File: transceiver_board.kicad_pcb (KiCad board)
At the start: 2 copper layers, 127 parts, among them J1 RJ45_LED_Shielded, J2 Conn_01x01_Male, J3 SMA_Connector, J4 Conn_01x01_Male, J5 SMA_Connector, Q1 BC547, Q2 BC547, T1 S558-5999-46-F, U1 LAN83C185-JT, U2 ltc6752ims8-2-pbf, U4 AP63203WU, U5 AP63205WU, U6 LM317_TO-220, U7 LM317_TO-220, Y1 25 MHz

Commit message: Begin placing components
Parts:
- moved C43 133.5 mm to (240.0, 150.0)
- moved RV1 133.3 mm to (236.3, 30.7), turned to 180 degrees
- moved C44 131.2 mm to (236.4, 149.4)
- moved R1 130.4 mm to (240.4, 152.6)
- moved R3 128.0 mm to (233.0, 151.6)
- moved C42 125.5 mm to (216.2, 151.0), turned to -90 degrees
- moved R2 121.1 mm to (212.0, 151.0), turned to 90 degrees
- moved C17 114.2 mm to (196.8, 147.4), turned to -90 degrees
- moved R46 112.0 mm to (210.8, 147.6)
- moved RV3 110.7 mm to (233.9, 155.7)
- moved R10 109.5 mm to (30.0, 74.0)
- moved R6 109.5 mm to (30.0, 76.9)
- moved C23 107.1 mm to (231.5, 45.8)
- moved U6 106.7 mm to (213.4, 140.8), turned to 180 degrees
- moved U7 105.1 mm to (234.9, 144.7)
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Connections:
- net PHY-VSS renamed GND
- Q1 pad 3: Net-(J3-Pad1) -> Net-(Q1-Pad3)
- Q2 pad 3: Net-(J3-Pad1) -> Net-(Q1-Pad3)

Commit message: positioned power components
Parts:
- removed R4: 0, Resistor_SMD:R_0805_2012Metric_Pad1.20x1.40mm_HandSolder
- added JP5: SolderJumper_2_Bridged, Jumper:SolderJumper-2_P1.3mm_Bridged_Pad1.0x1.5mm, F.Cu at (33.0, 108.5)
- moved C1 88.9 mm to (40.7, 144.5)
- moved C34 79.5 mm to (168.6, 152.9), turned to 180 degrees
- moved C35 78.8 mm to (44.8, 144.5), turned to 180 degrees
- moved U5 78.6 mm to (166.2, 155.8)
- moved C37 78.4 mm to (44.8, 142.2), turned to 180 degrees
- moved U4 74.7 mm to (42.5, 139.2)
- moved C32 72.9 mm to (164.1, 158.6)
- moved C45 72.5 mm to (40.7, 142.2)
- moved C36 71.1 mm to (168.3, 158.6), turned to 180 degrees
- moved C33 70.3 mm to (44.8, 136.4), turned to 180 degrees
- moved C38 69.0 mm to (168.3, 160.8), turned to 180 degrees
- moved L2 68.3 mm to (171.7, 155.7)
- moved L4 66.4 mm to (159.0, 154.9)
- moved L1 63.2 mm to (48.0, 139.7)
- moved L3 61.7 mm to (36.4, 138.9)
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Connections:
- C1 pad 2: GND -> PHY-VSS
- C10 pad 2: GND -> PHY-VSS
- C11 pad 2: GND -> PHY-VSS
- C12 pad 2: GND -> PHY-VSS
- C13 pad 2: GND -> PHY-VSS
- C14 pad 2: GND -> PHY-VSS
- C15 pad 2: GND -> PHY-VSS
- C16 pad 2: GND -> PHY-VSS
- C17 pad 2: GND -> PHY-VSS
- C18 pad 2: GND -> PHY-VSS
- C19 pad 2: GND -> PHY-VSS
- C20 pad 2: GND -> PHY-VSS
- C21 pad 2: GND -> PHY-VSS
- C22 pad 2: GND -> PHY-VSS
- C23 pad 2: GND -> PHY-VSS
- C24 pad 2: GND -> PHY-VSS
- C28 pad 2: GND -> PHY-VSS
- C29 pad 2: GND -> PHY-VSS
- C3 pad 2: GND -> PHY-VSS
- C30 pad 2: GND -> PHY-VSS
- C31 pad 2: GND -> PHY-VSS
- C32 pad 2: GND -> PHY-VSS
- C35 pad 2: GND -> PHY-VSS
- C36 pad 2: GND -> PHY-VSS
- C37 pad 2: GND -> PHY-VSS
- C38 pad 2: GND -> PHY-VSS
- C39 pad 2: GND -> PHY-VSS
- C4 pad 2: GND -> PHY-VSS
- C40 pad 2: GND -> PHY-VSS
- C41 pad 2: GND -> PHY-VSS
- C42 pad 2: GND -> PHY-VSS
- C43 pad 2: GND -> PHY-VSS
- C44 pad 2: GND -> PHY-VSS
- C45 pad 2: GND -> PHY-VSS
- C5 pad 2: GND -> PHY-VSS
- C6 pad 2: GND -> PHY-VSS
- C7 pad 2: GND -> PHY-VSS
- C8 pad 2: GND -> PHY-VSS
- C9 pad 2: GND -> PHY-VSS
- C_noise1 pad 2: GND -> PHY-VSS
- FPGA1 pad 25: GND -> PHY-VSS
- J4 pad 1: GND -> PHY-VSS
- R13 pad 1: GND -> PHY-VSS
- R14 pad 1: GND -> PHY-VSS
- R15 pad 1: GND -> PHY-VSS
- R17 pad 1: GND -> PHY-VSS
- R2 pad 1: GND -> PHY-VSS
- R22 pad 1: GND -> PHY-VSS
- R28 pad 2: GND -> PHY-VSS
- R3 pad 1: GND -> PHY-VSS
- R31 pad 2: GND -> PHY-VSS
- R33 pad 2: GND -> PHY-VSS
- R34 pad 2: GND -> PHY-VSS
- R35 pad 2: GND -> PHY-VSS
- RV1 pad 3: GND -> PHY-VSS
- RV2 pad 1: GND -> PHY-VSS
- RV3 pad 1: GND -> PHY-VSS
- R_L1 pad 2: GND -> PHY-VSS
- U1 pad 15: GND -> PHY-VSS
- U1 pad 21: GND -> PHY-VSS
- U1 pad 24: GND -> PHY-VSS
- U1 pad 28: GND -> PHY-VSS
- U1 pad 36: GND -> PHY-VSS
- U1 pad 40: GND -> PHY-VSS
- U1 pad 7: GND -> PHY-VSS
- U2 pad 6: GND -> PHY-VSS
- U4 pad 4: GND -> PHY-VSS
- U5 pad 4: GND -> PHY-VSS

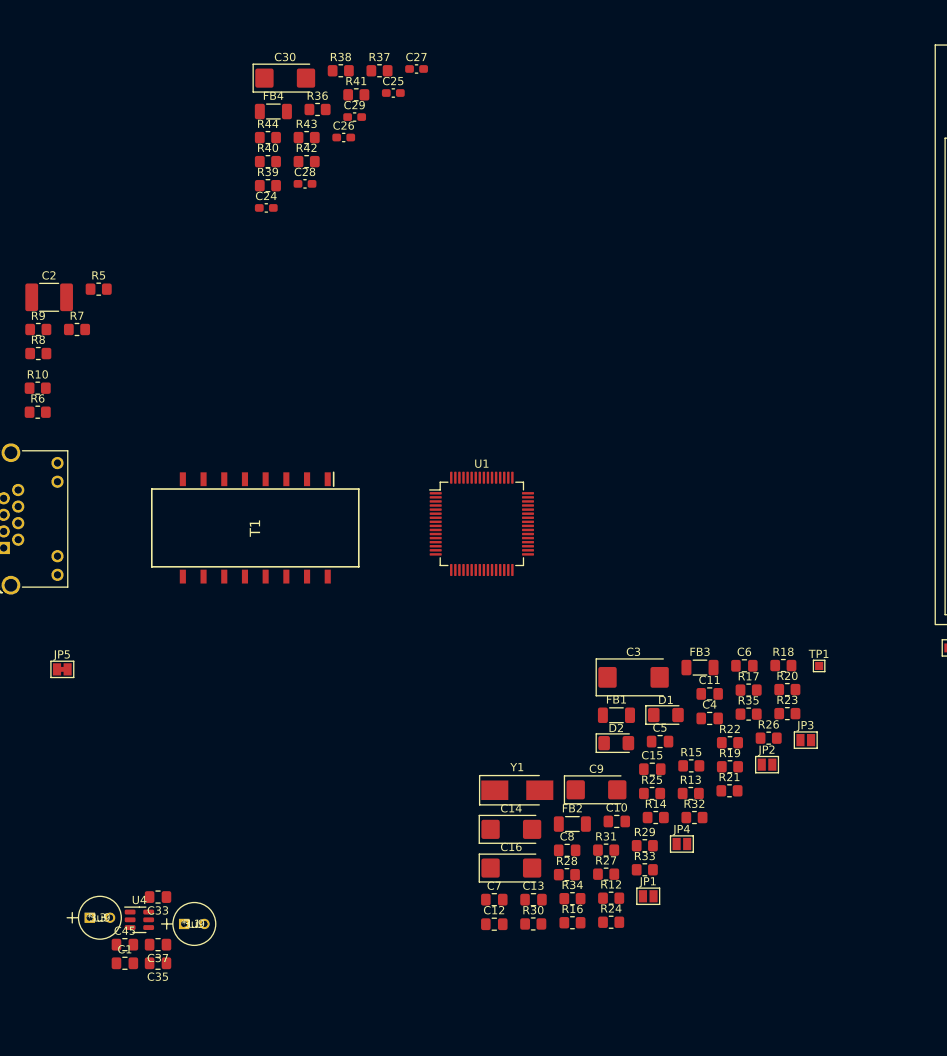
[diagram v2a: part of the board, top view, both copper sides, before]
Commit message: moved some resitors around to make myself feel better
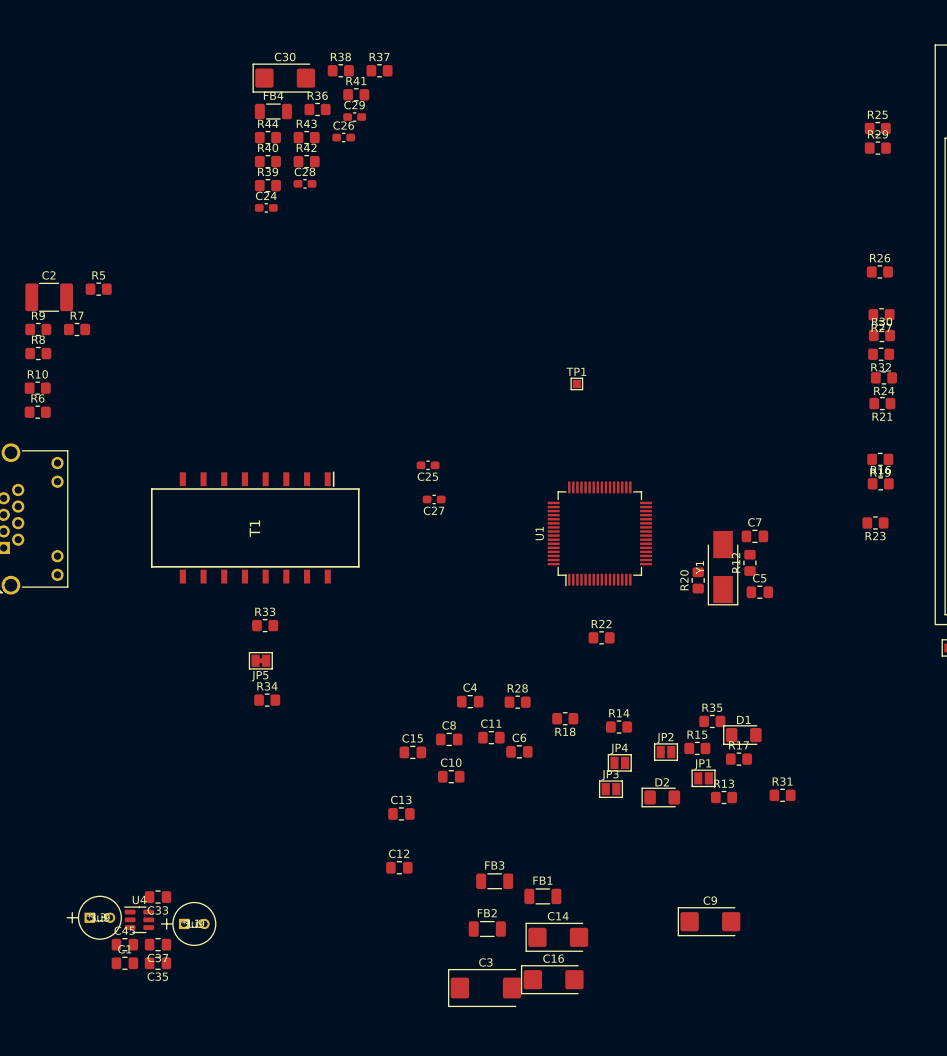
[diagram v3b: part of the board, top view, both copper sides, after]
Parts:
- moved R29 90.3 mm to (133.1, 44.5)
- moved R25 86.2 mm to (133.1, 42.1)
- moved R30 83.9 mm to (133.6, 67.5)
- moved R27 76.5 mm to (133.6, 64.9), turned to 180 degrees
- moved R24 74.7 mm to (133.8, 72.7), turned to 180 degrees
- moved R16 65.8 mm to (133.4, 85.7)
- moved R32 61.3 mm to (133.5, 69.8), turned to 180 degrees
- moved R26 58.8 mm to (133.3, 59.7)
- moved R33 55.4 mm to (57.9, 103.1)
- moved C7 54.9 mm to (118.0, 92.1)
- moved C27 52.9 mm to (78.7, 87.6), turned to 180 degrees
- moved R21 51.1 mm to (133.7, 75.8), turned to 180 degrees
- moved C25 45.9 mm to (77.9, 83.4), turned to 180 degrees
- moved TP1 45.6 mm to (96.2, 73.4)
- moved R34 44.7 mm to (58.2, 112.2)
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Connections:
- C1 pad 2: PHY-VSS -> PHY-AVSS
- C10 pad 2: PHY-VSS -> PHY-AVSS
- C11 pad 2: PHY-VSS -> PHY-AVSS
- C12 pad 2: PHY-VSS -> PHY-AVSS
- C13 pad 2: PHY-VSS -> PHY-AVSS
- C14 pad 2: PHY-VSS -> PHY-AVSS
- C15 pad 2: PHY-VSS -> PHY-AVSS
- C16 pad 2: PHY-VSS -> PHY-AVSS
- C17 pad 2: PHY-VSS -> PHY-AVSS
- C18 pad 2: PHY-VSS -> PHY-AVSS
- C19 pad 2: PHY-VSS -> PHY-AVSS
- C2 pad 2: PHY-AVSS -> GND1
- C20 pad 2: PHY-VSS -> PHY-AVSS
- C21 pad 2: PHY-VSS -> PHY-AVSS
- C22 pad 2: PHY-VSS -> PHY-AVSS
- C23 pad 2: PHY-VSS -> PHY-AVSS
- C24 pad 2: PHY-VSS -> PHY-AVSS
- C26 pad 2: PHY-AVSS -> GND1
- C28 pad 2: PHY-VSS -> PHY-AVSS
- C29 pad 2: PHY-VSS -> PHY-AVSS
- C3 pad 2: PHY-VSS -> PHY-AVSS
- C30 pad 2: PHY-VSS -> PHY-AVSS
- C31 pad 2: PHY-VSS -> PHY-AVSS
- C32 pad 2: PHY-VSS -> PHY-AVSS
- C35 pad 2: PHY-VSS -> PHY-AVSS
- C36 pad 2: PHY-VSS -> PHY-AVSS
- C37 pad 2: PHY-VSS -> PHY-AVSS
- C38 pad 2: PHY-VSS -> PHY-AVSS
- C39 pad 2: PHY-VSS -> PHY-AVSS
- C4 pad 2: PHY-VSS -> PHY-AVSS
- C40 pad 2: PHY-VSS -> PHY-AVSS
- C41 pad 2: PHY-VSS -> PHY-AVSS
- C42 pad 2: PHY-VSS -> PHY-AVSS
- C43 pad 2: PHY-VSS -> PHY-AVSS
- C44 pad 2: PHY-VSS -> PHY-AVSS
- C45 pad 2: PHY-VSS -> PHY-AVSS
- C5 pad 2: PHY-VSS -> PHY-AVSS
- C6 pad 2: PHY-VSS -> PHY-AVSS
- C7 pad 2: PHY-VSS -> PHY-AVSS
- C8 pad 2: PHY-VSS -> PHY-AVSS
- C9 pad 2: PHY-VSS -> PHY-AVSS
- C_noise1 pad 2: PHY-VSS -> PHY-AVSS
- FPGA1 pad 1: PHY-MDIO -> PHY-CRS
- FPGA1 pad 10: PHY-TX_ER -> PHY-RX_ER
- FPGA1 pad 11: PHY-TX_CLK -> PHY-RX_CLK
- FPGA1 pad 12: PHY-TX_EN -> PHY-RX_DV
- FPGA1 pad 13: PHY-COL -> PHY-RXD0
- FPGA1 pad 14: PHY-CRS -> PHY-RXD1
- FPGA1 pad 17: PHY-TXD0 -> PHY-RXD2
- FPGA1 pad 18: PHY-TXD1 -> PHY-RXD3
- FPGA1 pad 19: PHY-TXD2 -> PHY-MDC
- FPGA1 pad 2: PHY-MDC -> PHY-COL
- FPGA1 pad 20: PHY-TXD3 -> PHY-MDIO
- FPGA1 pad 25: PHY-VSS -> PHY-AVSS
- FPGA1 pad 3: PHY-RXD0 -> PHY-TXD3
- FPGA1 pad 4: PHY-RXD1 -> PHY-TXD2
- FPGA1 pad 5: PHY-RXD2 -> PHY-TXD1
- FPGA1 pad 6: PHY-RXD3 -> PHY-TXD0
- FPGA1 pad 7: PHY-RX_DV -> PHY-TX_EN
- FPGA1 pad 8: PHY-RX_CLK -> PHY-TX_CLK
- FPGA1 pad 9: PHY-RX_ER -> PHY-TX_ER
- J1 pad SH: PHY-AVSS -> GND1
- J4 pad 1: PHY-VSS -> PHY-AVSS
- JP5 pad 1: PHY-VSS -> PHY-AVSS
- JP5 pad 2: PHY-AVSS -> GND1
- Q1 pad 3: Net-(Q1-Pad3) -> Net-(J3-Pad1)
- Q2 pad 3: Net-(Q1-Pad3) -> Net-(J3-Pad1)
- R13 pad 1: PHY-VSS -> PHY-AVSS
- R14 pad 1: PHY-VSS -> PHY-AVSS
- R15 pad 1: PHY-VSS -> PHY-AVSS
- R17 pad 1: PHY-VSS -> PHY-AVSS
- R2 pad 1: PHY-VSS -> PHY-AVSS
- R22 pad 1: PHY-VSS -> PHY-AVSS
- R28 pad 2: PHY-VSS -> PHY-AVSS
- R3 pad 1: PHY-VSS -> PHY-AVSS
- R31 pad 2: PHY-VSS -> PHY-AVSS
- R33 pad 2: PHY-VSS -> PHY-AVSS
- R34 pad 2: PHY-VSS -> PHY-AVSS
- R35 pad 2: PHY-VSS -> PHY-AVSS
- RV1 pad 3: PHY-VSS -> PHY-AVSS
- RV2 pad 1: PHY-VSS -> PHY-AVSS
- RV3 pad 1: PHY-VSS -> PHY-AVSS
- R_L1 pad 2: PHY-VSS -> PHY-AVSS
- U1 pad 15: PHY-VSS -> PHY-AVSS
- U1 pad 21: PHY-VSS -> PHY-AVSS
- U1 pad 24: PHY-VSS -> PHY-AVSS
- U1 pad 28: PHY-VSS -> PHY-AVSS
- U1 pad 36: PHY-VSS -> PHY-AVSS
- U1 pad 40: PHY-VSS -> PHY-AVSS
- U1 pad 7: PHY-VSS -> PHY-AVSS
- U2 pad 6: PHY-VSS -> PHY-AVSS
- U4 pad 4: PHY-VSS -> PHY-AVSS
- U5 pad 4: PHY-VSS -> PHY-AVSS

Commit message: coppered the switching regs, moved through hole components to correct side of board
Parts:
- FPGA1, J2, J3, J4, J5, L1, L2, L3, L4, Q1, Q2, RV1, RV2, RV3, U6, U7: moved to B.Cu
- moved FPGA1 58.0 mm to (156.9, 98.3)
- moved R3 6.15 mm to (247.8, 146.6), turned to 90 degrees
- moved RV3 5.93 mm to (235.4, 155.8)
- moved RV2 5.16 mm to (208.2, 155.3)
- moved RV1 4.32 mm to (236.2, 26.4)
- moved L1 2.25 mm to (45.8, 139.1)
- moved L2 2.12 mm to (169.6, 155.7)
- moved L4 1.53 mm to (160.3, 155.8)
- moved U6 1.22 mm to (213.5, 142.0)
- moved D3 1.05 mm to (144.1, 105.3)
- moved J4 0.92 mm to (66.3, 174.5), turned to 180 degrees
- moved L3 0.38 mm to (36.7, 139.2)
- moved C5 0.27 mm to (118.3, 99.0)
- moved J2 0.20 mm to (43.1, 174.3), turned to 180 degrees
- turned J3 to 180 degrees
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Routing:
- net PHY-AVSS: track 0.00 -> 21.2 mm
- net +5V: track 0.00 -> 20.6 mm
- net +3V3: track 0.00 -> 20.5 mm
- net +12V: track 0.00 -> 14.0 mm
- net Net-(C45-Pad1): track 0.00 -> 5.07 mm
- net Net-(C34-Pad1): track 0.00 -> 5.06 mm
- net Net-(C32-Pad1): track 0.00 -> 5.05 mm
- net Net-(C33-Pad1): track 0.00 -> 2.75 mm
- net Net-(C34-Pad2): track 0.00 -> 1.98 mm
- net Net-(C33-Pad2): track 0.00 -> 1.82 mm

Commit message: Place and route optic side parts
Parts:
- removed C39: 2u2, Capacitor_Tantalum_SMD:CP_EIA-3528-15_AVX-H_Pad1.50x2.35mm_HandSolder
- removed C40, C41: 100n, Capacitor_SMD:C_0805_2012Metric_Pad1.18x1.45mm_HandSolder
- moved J2 181.2 mm to (204.2, 91.4)
- moved J4 171.4 mm to (216.2, 91.4)
- moved C1 152.7 mm to (185.6, 96.3), turned to 90 degrees
- moved C35 150.2 mm to (185.6, 92.2), turned to -90 degrees
- moved C45 149.8 mm to (183.3, 96.3), turned to 90 degrees
- moved L3 148.7 mm to (180.2, 100.3), turned to 90 degrees
- moved C37 147.3 mm to (183.3, 92.2), turned to -90 degrees
- moved U4 144.8 mm to (180.2, 94.5), turned to 90 degrees
- moved L1 142.7 mm to (180.2, 91.2), turned to 90 degrees
- moved C33 139.9 mm to (177.5, 92.2), turned to -90 degrees
- moved RV3 114.9 mm to (180.1, 55.1), turned to 90 degrees
- moved R1 110.9 mm to (185.2, 48.9), turned to 0 degrees
- moved C44 106.9 mm to (189.5, 48.9), turned to 0 degrees
- moved R3 105.6 mm to (186.0, 61.0), turned to 0 degrees
- moved U7 102.4 mm to (184.5, 55.0), turned to 0 degrees
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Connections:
- C1 pad 2: PHY-AVSS -> GND
- C10 pad 2: PHY-AVSS -> GND
- C11 pad 2: PHY-AVSS -> GND
- C12 pad 2: PHY-AVSS -> GND
- C13 pad 2: PHY-AVSS -> GND
- C14 pad 2: PHY-AVSS -> GND
- C15 pad 2: PHY-AVSS -> GND
- C16 pad 2: PHY-AVSS -> GND
- C17 pad 2: PHY-AVSS -> GND
- C18 pad 2: PHY-AVSS -> GND
- C19 pad 2: PHY-AVSS -> GND
- C20 pad 2: PHY-AVSS -> GND
- C21 pad 2: PHY-AVSS -> GND
- C22 pad 2: PHY-AVSS -> GND
- C23 pad 2: PHY-AVSS -> GND
- C24 pad 2: PHY-AVSS -> GND
- C28 pad 2: PHY-AVSS -> GND
- C29 pad 2: PHY-AVSS -> GND
- C3 pad 2: PHY-AVSS -> GND
- C30 pad 2: PHY-AVSS -> GND
- C31 pad 2: PHY-AVSS -> GND
- C32 pad 2: PHY-AVSS -> GND
- C35 pad 2: PHY-AVSS -> GND
- C36 pad 2: PHY-AVSS -> GND
- C37 pad 2: PHY-AVSS -> GND
- C38 pad 2: PHY-AVSS -> GND
- C4 pad 2: PHY-AVSS -> GND
- C42 pad 2: PHY-AVSS -> GND
- C43 pad 2: PHY-AVSS -> GND
- C44 pad 2: PHY-AVSS -> GND
- C45 pad 2: PHY-AVSS -> GND
- C5 pad 2: PHY-AVSS -> GND
- C6 pad 2: PHY-AVSS -> GND
- C7 pad 2: PHY-AVSS -> GND
- C8 pad 2: PHY-AVSS -> GND
- C9 pad 2: PHY-AVSS -> GND
- C_noise1 pad 2: PHY-AVSS -> GND
- FPGA1 pad 25: PHY-AVSS -> GND
- FPGA1 pad 33: unconnected-(FPGA1-Pad33) -> FPGA_TXn
- FPGA1 pad 35: FPGA_TXn -> FPGA_TXp
- FPGA1 pad 36: FPGA_TXp -> unconnected-(FPGA1-Pad36)
- FPGA1 pad 37: unconnected-(FPGA1-Pad37) -> Comparator_Output
- FPGA1 pad 39: Comparator_Output -> unconnected-(FPGA1-Pad39)
- J3 pad 3: (no net) -> GND
- J3 pad 4: (no net) -> GND
- J3 pad 5: (no net) -> GND
- J4 pad 1: PHY-AVSS -> GND
- J5 pad 3: (no net) -> Receiver_Output
- J5 pad 4: (no net) -> Receiver_Output
- J5 pad 5: (no net) -> Receiver_Output
- JP5 pad 1: PHY-AVSS -> GND
- R13 pad 1: PHY-AVSS -> GND
- R14 pad 1: PHY-AVSS -> GND
- R15 pad 1: PHY-AVSS -> GND
- R17 pad 1: PHY-AVSS -> GND
- R2 pad 1: PHY-AVSS -> GND
- R22 pad 1: PHY-AVSS -> GND
- R28 pad 2: PHY-AVSS -> GND
- R3 pad 1: PHY-AVSS -> GND
- R31 pad 2: PHY-AVSS -> GND
- R33 pad 2: PHY-AVSS -> GND
- R34 pad 2: PHY-AVSS -> GND
- R35 pad 2: PHY-AVSS -> GND
- RV1 pad 3: PHY-AVSS -> GND
- RV2 pad 1: PHY-AVSS -> GND
- RV3 pad 1: PHY-AVSS -> GND
- R_L1 pad 2: PHY-AVSS -> GND
- U1 pad 15: PHY-AVSS -> GND
- U1 pad 21: PHY-AVSS -> GND
- U1 pad 24: PHY-AVSS -> GND
- U1 pad 28: PHY-AVSS -> GND
- U1 pad 36: PHY-AVSS -> GND
- U1 pad 40: PHY-AVSS -> GND
- U1 pad 49: PHY-AVSS -> GND
- U1 pad 52: PHY-AVSS -> GND
- U1 pad 58: PHY-AVSS -> GND
- U1 pad 60: PHY-AVSS -> GND
- U1 pad 62: PHY-AVSS -> GND
- U1 pad 7: PHY-AVSS -> GND
- U2 pad 6: PHY-AVSS -> GND
- U4 pad 4: PHY-AVSS -> GND
- U5 pad 4: PHY-AVSS -> GND
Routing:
- net GND: track 0.00 -> 276.9 mm, vias 0 -> 4
- net +12V: track 14.0 -> 117.7 mm, vias 0 -> 1
- net +5V: track 20.6 -> 74.5 mm
- net Receiver_Output: track 0.00 -> 37.8 mm
- net /laser/High volt: track 0.00 -> 35.0 mm
- net Net-(J3-Pad1): track 0.00 -> 33.2 mm
- net /Comparator/trigger_voltage: track 0.00 -> 32.6 mm
- net FPGA_TXp: track 0.00 -> 22.2 mm
- net PHY-AVSS: track 21.2 -> 0.00 mm
- net /laser/Low volt: track 0.00 -> 17.2 mm
- net Net-(C_noise1-Pad1): track 0.00 -> 16.4 mm
- net FPGA_TXn: track 0.00 -> 15.1 mm
- net +3V3: track 20.5 -> 34.1 mm
- net Comparator_Output: track 0.00 -> 9.94 mm
- net Net-(RV2-Pad2): track 0.00 -> 8.43 mm
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
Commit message: did lots of routing for phy
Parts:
- added D4: Green LED, LED_SMD:LED_1206_3216Metric_Pad1.42x1.75mm_HandSolder, F.Cu at (111.5, 107.5)
- added D5: Yellow LED, LED_SMD:LED_1206_3216Metric_Pad1.42x1.75mm_HandSolder, F.Cu at (117.2, 107.5)
- J1: value RJ45_LED_Shielded -> 85505-5113; footprint Connector_RJ:RJ45_Amphenol_RJHSE538X -> KiCad 85505-5113:85505-5113_1; moved to B.Cu
- moved C30 74.4 mm to (71.5, 109.5), turned to -90 degrees
- moved C29 70.2 mm to (61.9, 110.5), turned to 180 degrees
- moved FB4 68.9 mm to (66.8, 108.5), turned to 90 degrees
- moved R42 60.3 mm to (62.0, 106.5), turned to 180 degrees
- moved R44 59.5 mm to (66.0, 102.2), turned to 90 degrees
- moved R34 59.1 mm to (117.2, 113.2), turned to -90 degrees
- moved R43 59.0 mm to (63.0, 102.2), turned to 90 degrees
- moved R33 54.5 mm to (111.5, 113.2), turned to -90 degrees
- moved C28 53.7 mm to (59.5, 102.5), turned to 180 degrees
- moved R36 52.7 mm to (73.2, 91.7), turned to 180 degrees
- moved R37 47.0 mm to (82.8, 80.7), turned to 90 degrees
- moved C8 46.0 mm to (98.5, 74.7), turned to 90 degrees
- moved R38 44.6 mm to (54.5, 77.7), turned to 90 degrees
- moved R41 43.6 mm to (51.2, 77.7), turned to -90 degrees
- moved R18 42.8 mm to (133.2, 95.6)
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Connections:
- FPGA1 pad 1: PHY-CRS -> PHY-MDIO
- FPGA1 pad 10: PHY-RX_ER -> PHY-TX_ER
- FPGA1 pad 11: PHY-RX_CLK -> PHY-TX_CLK
- FPGA1 pad 12: PHY-RX_DV -> PHY-TX_EN
- FPGA1 pad 13: PHY-RXD0 -> PHY-TXD0
- FPGA1 pad 14: PHY-RXD1 -> PHY-TXD1
- FPGA1 pad 15: unconnected-(FPGA1-Pad15) -> PHY-TXD2
- FPGA1 pad 16: unconnected-(FPGA1-Pad16) -> PHY-TXD3
- FPGA1 pad 17: PHY-RXD2 -> PHY-COL
- FPGA1 pad 18: PHY-RXD3 -> PHY-CRS
- FPGA1 pad 19: PHY-MDC -> unconnected-(FPGA1-Pad19)
- FPGA1 pad 2: PHY-COL -> PHY-MDC
- FPGA1 pad 20: PHY-MDIO -> unconnected-(FPGA1-Pad20)
- FPGA1 pad 3: PHY-TXD3 -> PHY-RXD3
- FPGA1 pad 4: PHY-TXD2 -> PHY-RXD2
- FPGA1 pad 5: PHY-TXD1 -> PHY-RXD1
- FPGA1 pad 6: PHY-TXD0 -> PHY-RXD0
- FPGA1 pad 7: PHY-TX_EN -> PHY-RX_DV
- FPGA1 pad 8: PHY-TX_CLK -> PHY-RX_CLK
- FPGA1 pad 9: PHY-TX_ER -> PHY-RX_ER
- J1 pad 10: ETH-L1P -> (no net)
- J1 pad 11: ETH-L2N -> GND1
- J1 pad 12: ETH-L2P -> GND1
- J1 pad 7: Net-(J1-Pad7) -> Net-(R7-Pad1)
- J1 pad 8: Net-(J1-Pad8) -> Net-(R5-Pad1)
- J1 pad 9: ETH-L1N -> (no net)
- R18 pad 1: +3V3 -> PHY-VREG
- R33 pad 1: ETH-L1N -> Net-(R33-Pad1)
- R34 pad 1: ETH-L2N -> Net-(R34-Pad1)
- R5 pad 1: Net-(J1-Pad7) -> Net-(R5-Pad1)
- R7 pad 1: Net-(J1-Pad8) -> Net-(R7-Pad1)
- U1 pad 17: ETH-L1P -> PHY-AD1
- U1 pad 19: ETH-L2P -> PHY-AD2
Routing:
- net GND: track 276.9 -> 520.1 mm, vias 4 -> 10
- net PHY-TXD3: track 0.00 -> 86.5 mm
- net PHY-TXD2: track 0.00 -> 85.8 mm
- net PHY-TXD1: track 0.00 -> 82.3 mm
- net PHY-TXD0: track 0.00 -> 82.0 mm
- net PHY-TX_EN: track 0.00 -> 80.2 mm
- net PHY-TX_ER: track 0.00 -> 76.4 mm
- net MAG-TXn: track 0.00 -> 75.8 mm
- net MAG-TXp: track 0.00 -> 73.6 mm
- net Net-(R25-Pad1): track 0.00 -> 66.8 mm
- net Net-(R29-Pad1): track 0.00 -> 64.3 mm
- net PHY-MDC: track 0.00 -> 61.0 mm
- net PHY-AVDD: track 0.00 -> 49.3 mm, vias 0 -> 3
- net Net-(R26-Pad1): track 0.00 -> 46.2 mm
- net PHY-VDD: track 0.00 -> 46.1 mm, vias 0 -> 2
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
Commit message: did a lot more routing, phy nearly done
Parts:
- moved FB3 48.5 mm to (127.4, 109.0), turned to 90 degrees
- moved C16 48.0 mm to (122.1, 108.1), turned to 90 degrees
- moved C14 44.2 mm to (78.0, 100.1), turned to -90 degrees
- moved FB2 39.4 mm to (83.0, 101.0), turned to 90 degrees
- moved C9 37.4 mm to (98.2, 112.0), turned to 180 degrees
- moved C3 36.4 mm to (85.9, 111.1), turned to -90 degrees
- moved FB1 29.4 mm to (108.5, 112.0), turned to 180 degrees
- moved R29 25.0 mm to (150.0, 62.9)
- moved R26 24.9 mm to (150.0, 78.2)
- moved R25 24.9 mm to (150.0, 60.4)
- moved R32 24.9 mm to (150.0, 88.4)
- moved R27 24.6 mm to (150.0, 83.2)
- moved R30 24.5 mm to (150.0, 85.8)
- moved R24 24.3 mm to (150.0, 90.9)
- moved R21 24.1 mm to (150.0, 93.5)
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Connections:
- net MAG-RXn renamed MAG-RXN
- net MAG-RXp renamed MAG-RXP
- net MAG-TXn renamed MAG-TXN
- net MAG-TXp renamed MAG-TXP
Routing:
- net GND: track 520.1 -> 789.4 mm, vias 10 -> 7
- net +3V3: track 34.1 -> 164.0 mm
- net PHY-VDD: track 46.1 -> 136.9 mm, vias 2 -> 5
- net PHY-AVDD: track 49.3 -> 95.2 mm, vias 3 -> 1
- net PHY-VREG: track 10.7 -> 56.0 mm, vias 1 -> 2
- net Net-(R23-Pad2): track 32.2 -> 71.4 mm
- net Net-(R16-Pad2): track 31.2 -> 68.4 mm
- net Net-(R19-Pad2): track 31.4 -> 66.7 mm
- net Net-(R21-Pad2): track 34.5 -> 65.0 mm
- net Net-(R24-Pad2): track 35.5 -> 63.7 mm
- net Net-(R32-Pad2): track 36.4 -> 63.3 mm
- net Net-(R30-Pad2): track 38.4 -> 63.2 mm
- net PHY-COL: track 30.3 -> 5.81 mm
- net PHY-CRS: track 30.3 -> 5.79 mm
- net PHY-TX_CLK: track 30.1 -> 5.80 mm
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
